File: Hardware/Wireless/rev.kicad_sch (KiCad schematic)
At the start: 72 parts, among them J2 Conn_01x02_Pin, J3 Conn_01x02_Pin, J4 Conn_01x04_Socket, Q1 NMOS-CSD17381F4, Q2 NMOS-CSD17381F4, Q3 PMOS-CSD25483F4, Q4 PMOS-CSD25483F4, Q5 PMOS-CSD25483F4, SW4 SW_Push, SW5 SW_DPDT_x2, U1 BQ27427, U2 nrf52833_qfn40, U3 Conn_01x14_Socket, U4 TPS709, U5 AS5600, U6 BQ25180, U7 LSM6DSO, U8 TS5A3159AYZPR, U9 TPS22910A, X1 32.768 kHz, X2 32MHZ

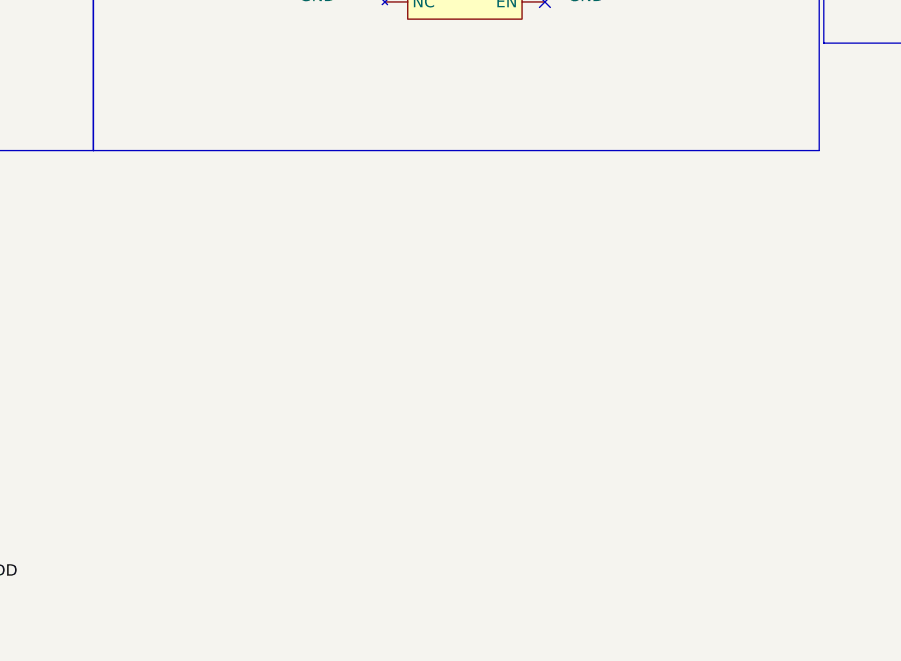
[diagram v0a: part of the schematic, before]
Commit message: added TLV493D sensor
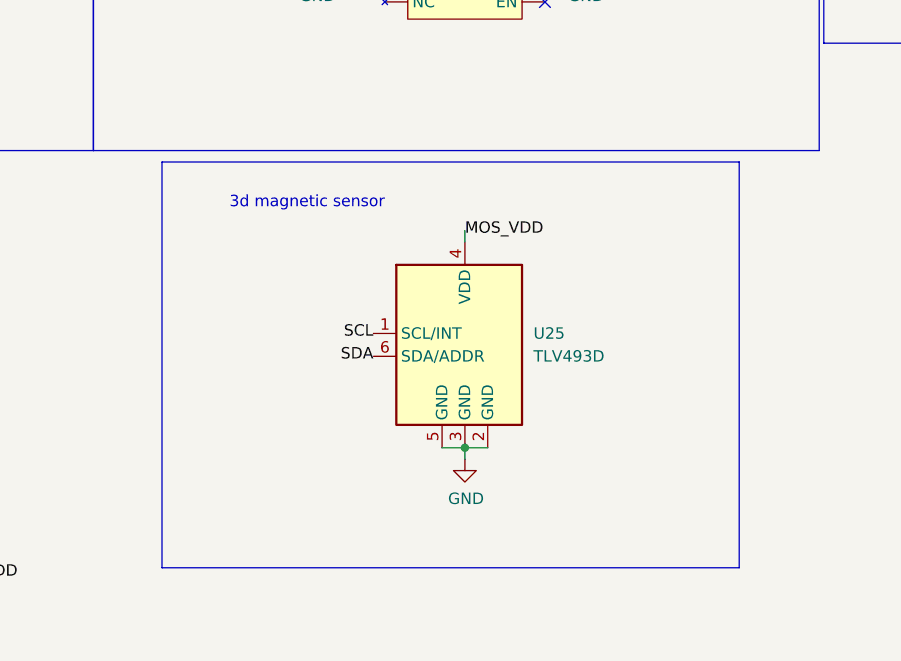
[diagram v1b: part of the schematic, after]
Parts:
- added U25: TLV493D, Library:SOT-23-6-Small, symbol Sensor_Magnetic:TLV493D
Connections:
- net GND: now also U25.2 (GND), U25.3 (GND), U25.5 (GND)
- net MOS_VDD: now also U25.4 (VDD)
- net P0.15: now also U25.1 (SCL/INT)
- net P0.17: now also U25.6 (SDA/ADDR)
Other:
- note added: "3d magnetic sensor"

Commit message: route
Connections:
- net P0.17: now also J4.4 (Pin_4)
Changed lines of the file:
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@@
 	)
 	(label "SDA"
-		(at 132.715 259.08 270)
+		(at 132.08 259.08 270)
 		(fields_autoplaced yes)
 		(effects
@@
 		)
 		(property "Intersheetrefs" "${INTERSHEET_REFS}"
-			(at 132.715 265.6333 90)
+			(at 132.08 265.6333 90)
 			(effects
 				(font

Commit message: finished routing
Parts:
- added TP12, TP13, TP14, TP15, TP18, TP4: TestPoint, TestPoint:TestPoint_Pad_D1.0mm, symbol Connector:TestPoint
- R14: value 50r -> *50r
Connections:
- net Batteryin: now also TP18.1
- net COM: now also U8.A1, TP12.1; no longer R14.2, U8.C2
- net MOS_VDD: now also TP14.1
- net P0.15: now also R8.1, U6.B1 (SCL); no longer R9.1, U6.C1 (SDA)
- net P0.17: now also R9.1, U6.C1 (SDA); no longer R8.1, U6.B1 (SCL)
- net TX_TS5A3159AYZPR: now also R14.2, U8.C2; no longer U8.A1
- net VDD_nRF: now also TP15.1
- net vBAT: now also TP13.1
- net vSYSTEM: now also TP4.1

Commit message: update kicad 9
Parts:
- AE1, BT1, C19, C8, J2, J3, J4, JP1, Q1, Q2, Q3, Q4, Q5, R10, R14, SW4, SW5, U1, U25, U3, U4, U6, U7, U8, U9: ID (none) -> 0
- C11, C18, C4: value 100nF -> 100nf
- C21, C24, C26: footprint Capacitor_SMD:C_0402_1005Metric -> Library:0402; ID (none) -> 30
- C23: footprint Capacitor_SMD:C_0402_1005Metric -> Library:0402; ID (none) -> 83
- C25: value 100nF -> 100nf; footprint Capacitor_SMD:C_0402_1005Metric -> Library:0402; ID (none) -> 21
- C27: footprint Capacitor_SMD:C_0402_1005Metric -> Library:0402; ID (none) -> 21
- R11, R12: ID 135 -> 29
- R13: value 10k -> 10K; ID (none) -> 7
- R3: value 10k -> 10K; ID 110 -> 7
- R4, R5: value 1.5k -> 1.5K; ID 138 -> 27
- R6: ID 105 -> 8
- R8, R9, TH1: ID (none) -> 7
- TP12, TP13, TP14, TP15, TP18, TP2, TP3, TP4: ID (none) -> 0; now not fitted
- X2: ID 42 -> 33
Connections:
- net D-: now also U2.12 (D-)
- net d+: now also U2.13 (D+)
